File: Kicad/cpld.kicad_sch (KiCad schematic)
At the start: 16 parts, among them J2 Conn_01x06_Pin, U7 AMS1117-3.3, U9 XC95144XL-TQ144

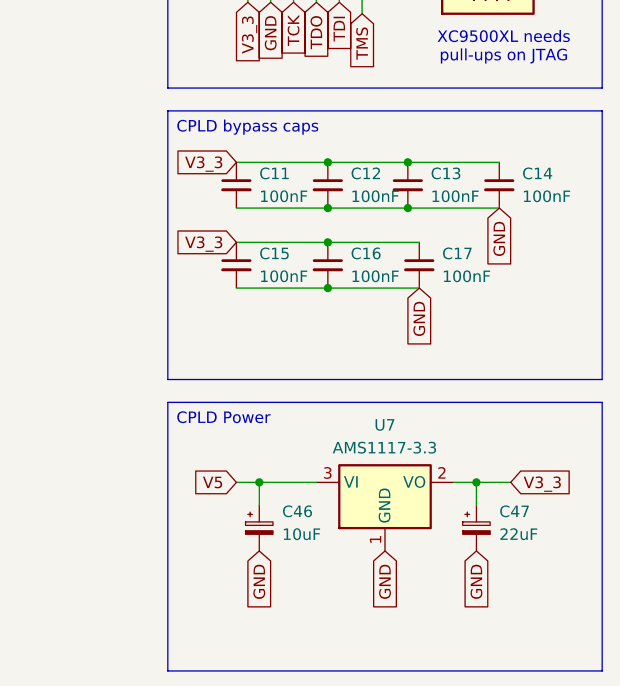
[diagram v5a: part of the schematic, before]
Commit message: Rename capacitors
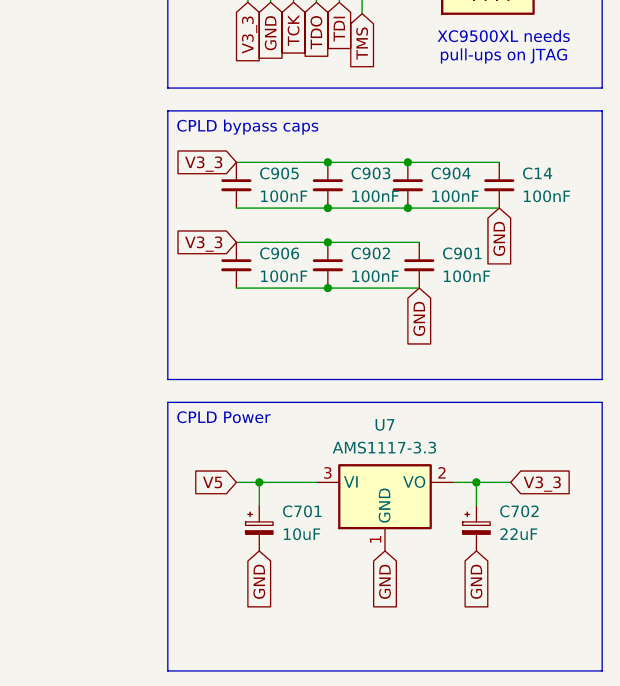
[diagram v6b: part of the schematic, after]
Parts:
- renumbered C46 to C701, C47 to C702, C17 to C901, C16 to C902, C12 to C903, C13 to C904, C11 to C905, C15 to C906
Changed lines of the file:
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@@
 		(dnp no)
 		(fields_autoplaced yes)
-		(property "Reference" "C15"
+		(property "Reference" "C906"
 			(at 160.02 67.3162 0)
 			(effects
@@
 			(project "A4092"
 				(path "/8f9f4021-47aa-41d9-bea7-f6ccf72098bb/6ae4417c-9681-4757-b289-033d6e31deb3"
-					(reference "C15")
+					(reference "C906")
 					(unit 1)
 				)
@@
 		(dnp no)
 		(fields_autoplaced yes)
-		(property "Reference" "C46"
+		(property "Reference" "C701"
 			(at 162.56 95.9738 0)
 			(effects
@@
 			(project "A4092"
 				(path "/8f9f4021-47aa-41d9-bea7-f6ccf72098bb/6ae4417c-9681-4757-b289-033d6e31deb3"
-					(reference "C46")
+					(reference "C701")
 					(unit 1)
 				)
@@
 		(dnp no)
 		(fields_autoplaced yes)
-		(property "Reference" "C17"
+		(property "Reference" "C901"
 			(at 180.34 67.3162 0)
 			(effects
@@
 			(project "A4092"
 				(path "/8f9f4021-47aa-41d9-bea7-f6ccf72098bb/6ae4417c-9681-4757-b289-033d6e31deb3"
-					(reference "C17")
+					(reference "C901")
 					(unit 1)
 				)
@@
 		(dnp no)
 		(fields_autoplaced yes)
-		(property "Reference" "C13"
+		(property "Reference" "C904"
 			(at 179.07 58.4262 0)
 			(effects
@@
 			(project "A4092"
 				(path "/8f9f4021-47aa-41d9-bea7-f6ccf72098bb/6ae4417c-9681-4757-b289-033d6e31deb3"
-					(reference "C13")
+					(reference "C904")
 					(unit 1)
 				)
@@
 		(dnp no)
 		(fields_autoplaced yes)
-		(property "Reference" "C11"
+		(property "Reference" "C905"
 			(at 160.02 58.4262 0)
 			(effects
@@
 			(project ""
 				(path "/8f9f4021-47aa-41d9-bea7-f6ccf72098bb/6ae4417c-9681-4757-b289-033d6e31deb3"
-					(reference "C11")
+					(reference "C905")
 					(unit 1)
 				)
@@
 		(dnp no)
 		(fields_autoplaced yes)
-		(property "Reference" "C47"
+		(property "Reference" "C702"
 			(at 186.69 95.9738 0)
 			(effects
@@
 			(project "A4092"
 				(path "/8f9f4021-47aa-41d9-bea7-f6ccf72098bb/6ae4417c-9681-4757-b289-033d6e31deb3"
-					(reference "C47")
+					(reference "C702")
 					(unit 1)
 				)
@@
 		(dnp no)
 		(fields_autoplaced yes)
-		(property "Reference" "C12"
+		(property "Reference" "C903"
 			(at 170.18 58.4262 0)
 			(effects
@@
 			(project ""
 				(path "/8f9f4021-47aa-41d9-bea7-f6ccf72098bb/6ae4417c-9681-4757-b289-033d6e31deb3"
-					(reference "C12")
+					(reference "C903")
 					(unit 1)
 				)
@@
 		(dnp no)
 		(fields_autoplaced yes)
-		(property "Reference" "C16"
+		(property "Reference" "C902"
 			(at 170.18 67.3162 0)
 			(effects
@@
 			(project "A4092"
 				(path "/8f9f4021-47aa-41d9-bea7-f6ccf72098bb/6ae4417c-9681-4757-b289-033d6e31deb3"
-					(reference "C16")
-					(unit 1)
-				)
+					(reference "C902")
+					(unit 1)
+				)

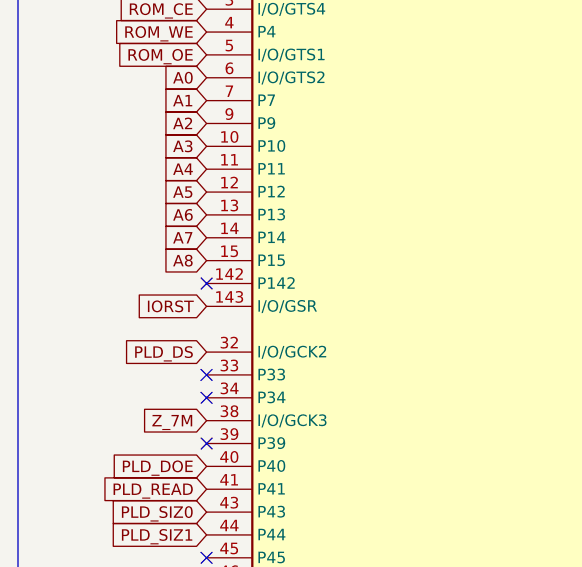
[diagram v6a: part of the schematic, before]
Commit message: Connect SC0 from 53c710 to CPLD
This will let us implement the "False DMA Request Bugfix"
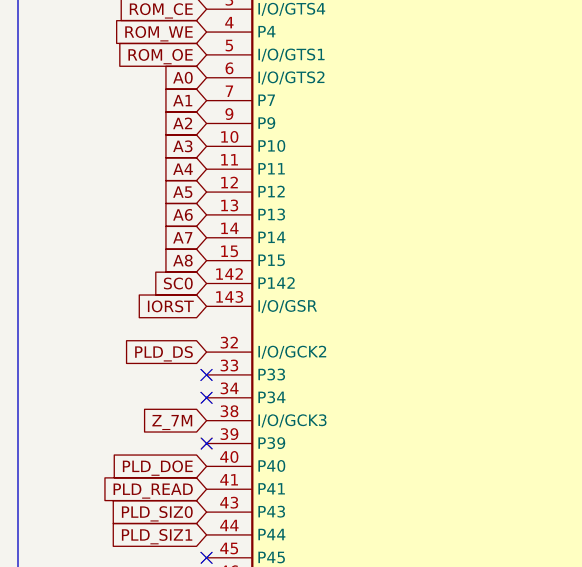
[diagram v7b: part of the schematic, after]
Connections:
- net SC0: now reaches U9.142 (P142)
- no-connect marks 30 -> 29
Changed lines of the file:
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@@
-	)
-	(no_connect
-		(at 34.29 96.52)
 	)
 	(no_connect
@@
 			(effects
 				(font
+					(size 1.27 1.27)
+				)
+				(justify right)
+				(hide yes)
+			)
+		)
+	)
+	(global_label "SC0"
+		(shape input)
+		(at 34.29 96.52 180)
+		(fields_autoplaced yes)
+		(effects
+			(font
+				(size 1.27 1.27)
+			)
+			(justify right)
+		)
+		(property "Intersheetrefs" "${INTERSHEET_REFS}"
+			(at 27.6158 96.52 0)
+			(effects
+				(font

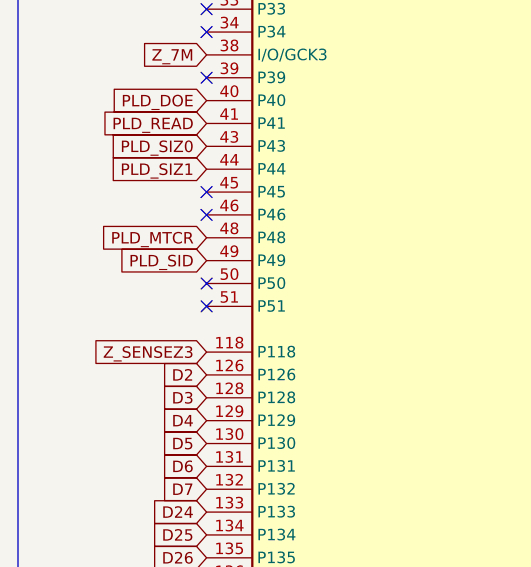
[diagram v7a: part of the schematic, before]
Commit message: Connect DIP_EXT_TERM to CPLD
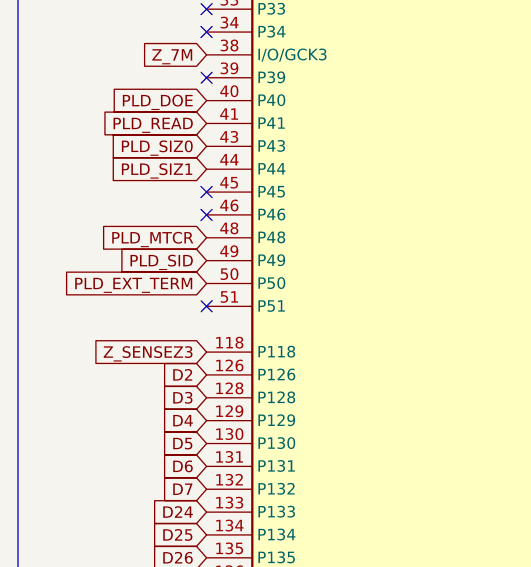
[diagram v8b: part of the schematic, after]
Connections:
- net PLD_EXT_TERM: now reaches U9.50 (P50)
- no-connect marks 29 -> 28
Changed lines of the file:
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@@
-	)
-	(no_connect
-		(at 34.29 137.16)
 	)
 	(no_connect
@@
 				(hide yes)
 			)
+		)
+	)
+	(global_label "PLD_EXT_TERM"
+		(shape input)
+		(at 34.29 137.16 180)
+		(fields_autoplaced yes)
+		(effects
+			(font
+				(size 1.27 1.27)
+			)
+			(justify right)
+		)
+		(property "Intersheetrefs" "${INTERSHEET_REFS}"
+			(at 17.6374 137.16 0)
+			(effects
+				(font
+					(size 1.27 1.27)
+				)
+				(justify right)
+				(hide yes)
+			)
